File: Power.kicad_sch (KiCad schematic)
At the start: 21 parts, among them J1 ATX-24, J5 USB_C_Receptacle_USB2.0_16P, Q1 MMBT3904, U2 AMS1117-3.3, U5 74LVC1G02, U7 74LVC1G02

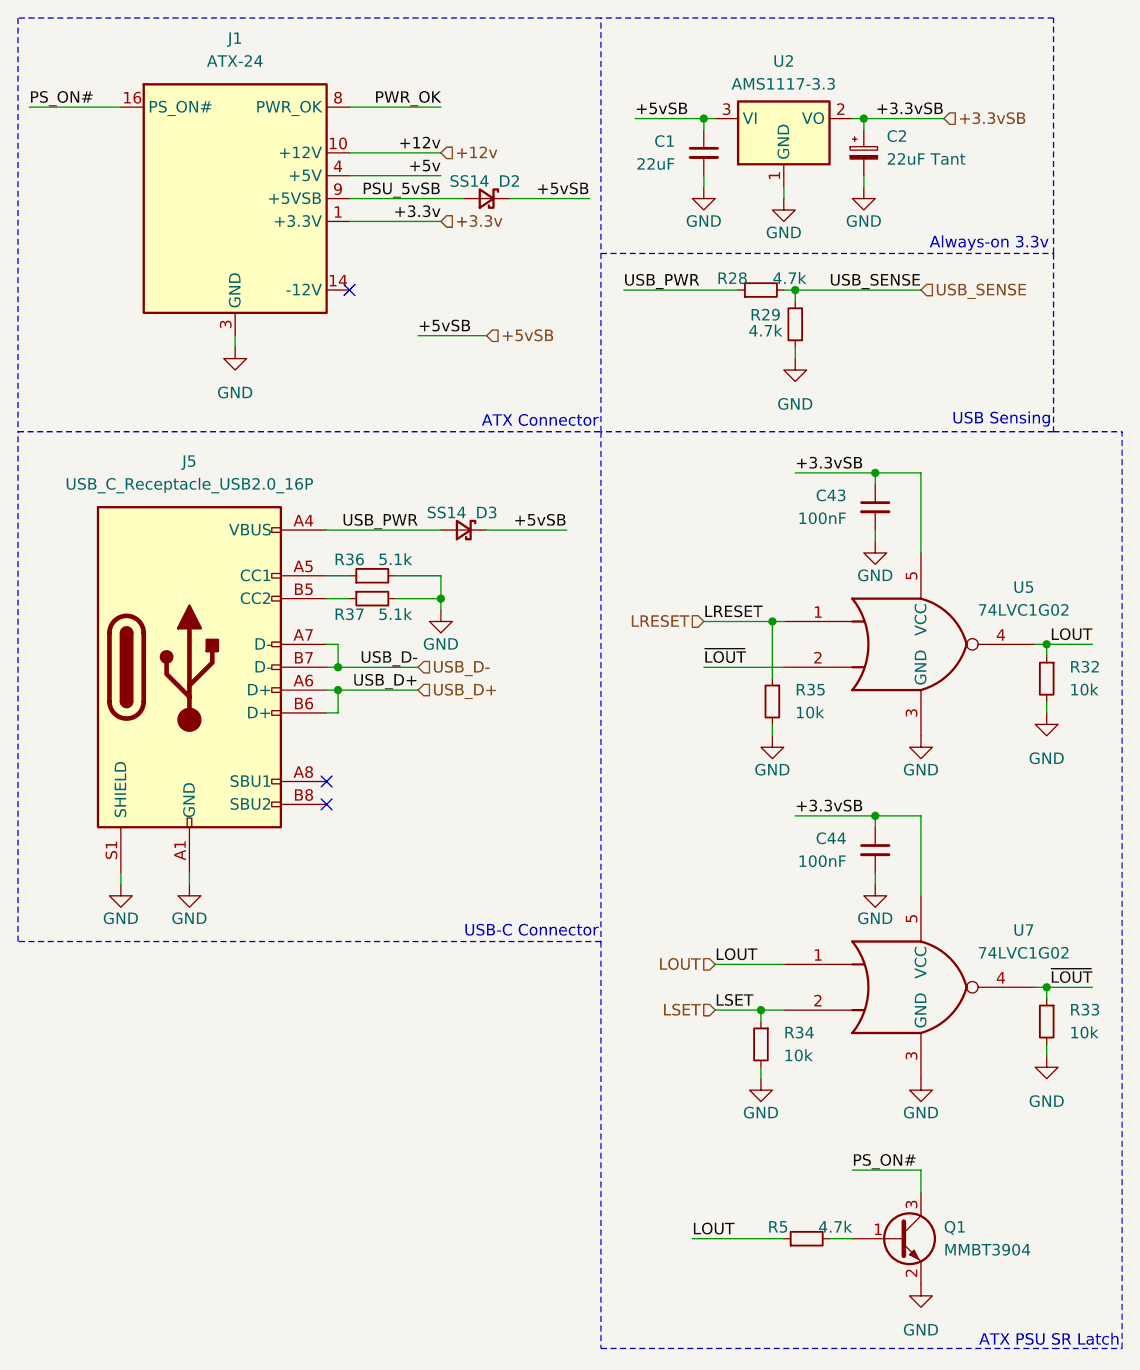
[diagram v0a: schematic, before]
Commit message: rev5
Added MACROM (specific ROM holding MAC address and (optionally) board
revision)
Added more circuitry to protect the EMC2301, allowing for use with fans
with internal pull-ups.
Added USB-C
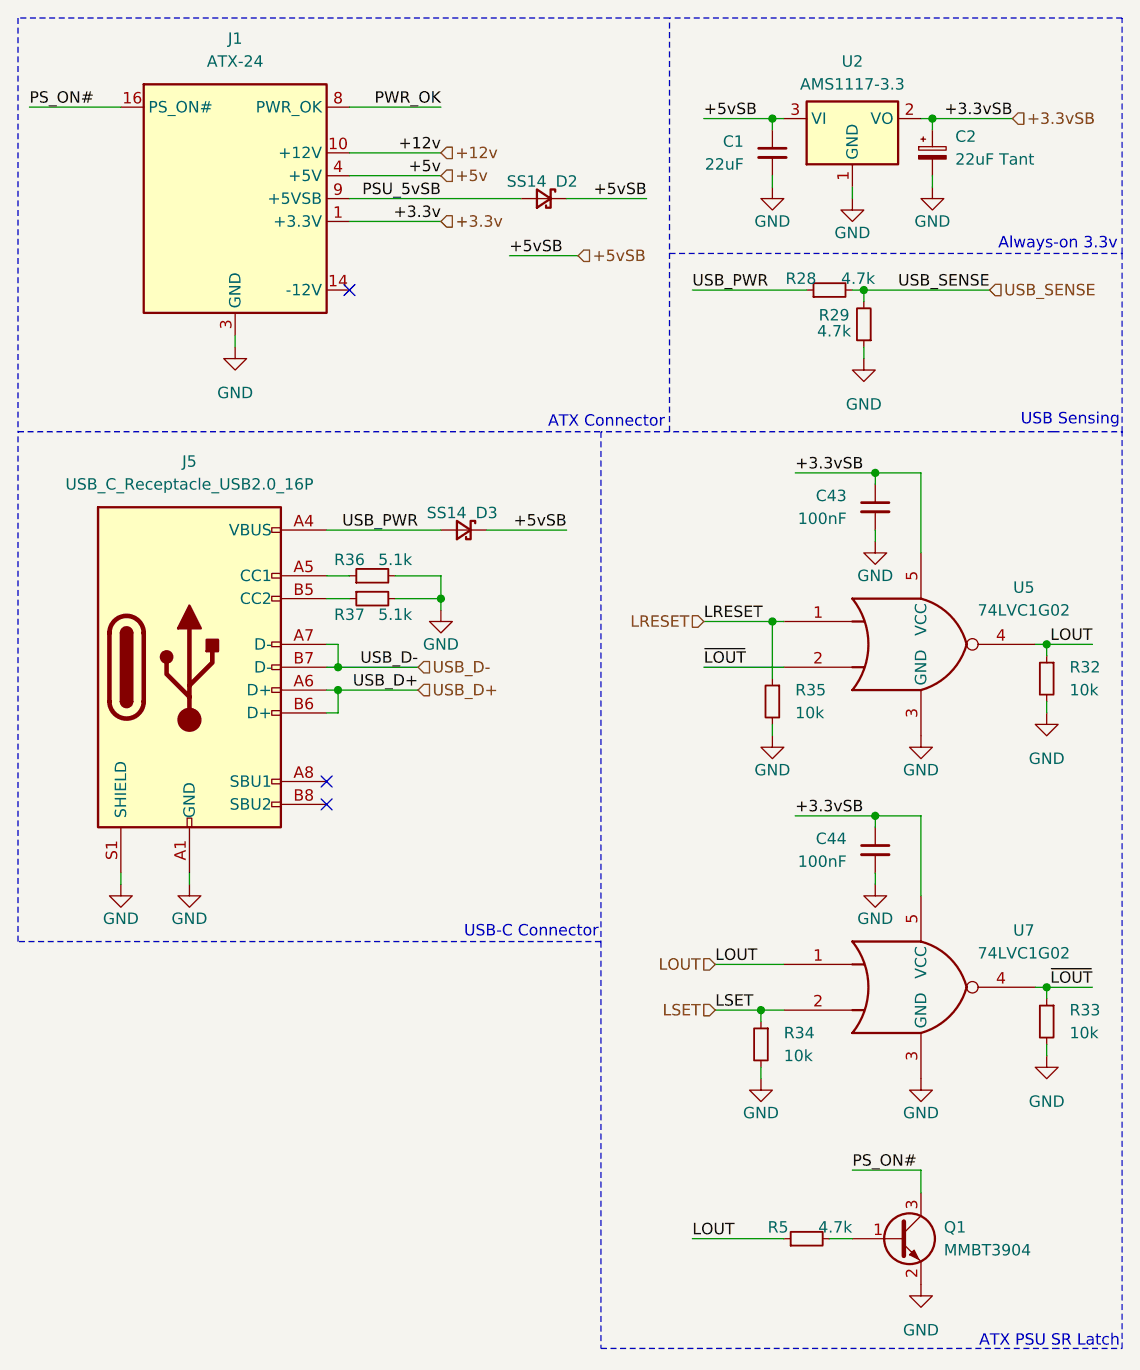
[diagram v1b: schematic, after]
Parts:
- C1: JLCPCB_PN C12891 -> (none); LCSC Part # (none) -> C12891
- C2: JLCPCB_PN C11366 -> (none); LCSC Part # (none) -> C11366
- C43, C44: JLCPCB_PN C1525 -> (none); LCSC Part # (none) -> C1525
- D2, D3: JLCPCB_PN C2480 -> (none); LCSC Part # (none) -> C2480
- J1: JLCPCB_PN C492535 -> (none); LCSC Part # (none) -> C492535
- J5: JLCPCB_PN C393939 -> (none); LCSC Part # (none) -> C393939
- Q1: JLCPCB_PN C20526 -> (none); LCSC Part # (none) -> C20526
- R28, R29, R5: JLCPCB_PN C25900 -> (none); LCSC Part # (none) -> C25900
- R32, R33, R34, R35: LCSC Part # (none) -> C25744
- R36, R37: LCSC Part # (none) -> C25905
- U2: JLCPCB_PN C6186 -> (none); LCSC Part # (none) -> C6186
- U5, U7: JLCPCB_PN C353856 -> (none); LCSC Part # (none) -> C353856
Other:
- moved on the sheet: C1, C2, D2, R28, R29, U2
